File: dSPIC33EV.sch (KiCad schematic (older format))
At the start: 45 parts, among them J5 CONN_01X05, J6 test, J7 CONN_01X05, J8 CONN_COAXIAL, J9 DB9_Female_MountingHoles, SW1 SW_Push, U4 74LS04, U5 dsPIC33EV256GM002, U6 SN75451, U7 MAX232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

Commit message: 저항값설정
저항값 1차 설정
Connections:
- wire segments 158 -> 156
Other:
- note added: "RX Selection : R14 for optic interface, R12 RS232C interface. \nBetween them only one shoud be shorted"
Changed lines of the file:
@@
 Connection ~ 1900 9100
-Wire Wire Line
-	2650 9150 2650 9100
-Connection ~ 2650 9100
 Wire Wire Line
 	2400 9150 2400 9100
@@
 	2900 9500 2900 9450
 Connection ~ 1900 9500
-Wire Wire Line
-	2650 9450 2650 9500
-Connection ~ 2650 9500
 Wire Wire Line
 	2400 9450 2400 9500
@@
 Wire Wire Line
 	1750 7300 1900 7300
+Text Notes 8600 5550 0    60   ~ 0
+RX Selection : R14 for optic interface, R12 RS232C interface. \nBetween them only one shoud be shorted
 $EndSCHEMATC

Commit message: 전해콘덴서 foot print 변경
전해 콘덴서 변경
Bypass 콘데서 OPAMP에 추가 하여야 함
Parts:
- C28, C32, C34, C36, C39, C40, C41: footprint Capacitors_SMD:C_1812_HandSoldering -> USER:C_1812_HandSoldering_Polar
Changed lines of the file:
@@
 F 0 "C36" H 10775 6500 50  0000 L CNN
 F 1 "10uF" H 10775 6300 50  0000 L CNN
-F 2 "Capacitors_SMD:C_1812_HandSoldering" H 10750 6400 50  0001 C CNN
+F 2 "USER:C_1812_HandSoldering_Polar" H 10750 6400 50  0001 C CNN
 F 3 "" H 10750 6400 50  0001 C CNN
 	1    10750 6400
@@
 F 0 "C41" H 13125 7150 50  0000 L CNN
 F 1 "10uF" H 13125 6950 50  0000 L CNN
-F 2 "Capacitors_SMD:C_1812_HandSoldering" H 13100 7050 50  0001 C CNN
+F 2 "USER:C_1812_HandSoldering_Polar" H 13100 7050 50  0001 C CNN
 F 3 "" H 13100 7050 50  0001 C CNN
 	1    13100 7050
@@
 F 0 "C39" H 13075 6500 50  0000 L CNN
 F 1 "10uF" H 13075 6300 50  0000 L CNN
-F 2 "Capacitors_SMD:C_1812_HandSoldering" H 13050 6400 50  0001 C CNN
+F 2 "USER:C_1812_HandSoldering_Polar" H 13050 6400 50  0001 C CNN
 F 3 "" H 13050 6400 50  0001 C CNN
 	1    13050 6400
@@
 F 0 "C40" H 13125 6850 50  0000 L CNN
 F 1 "10uF" H 13125 6650 50  0000 L CNN
-F 2 "Capacitors_SMD:C_1812_HandSoldering" H 13100 6750 50  0001 C CNN
+F 2 "USER:C_1812_HandSoldering_Polar" H 13100 6750 50  0001 C CNN
 F 3 "" H 13100 6750 50  0001 C CNN
 	1    13100 6750
@@
 F 0 "C28" H 3525 3400 50  0000 L CNN
 F 1 "10uF" H 3525 3200 50  0000 L CNN
-F 2 "Capacitors_SMD:C_1812_HandSoldering" H 3500 3300 50  0001 C CNN
+F 2 "USER:C_1812_HandSoldering_Polar" H 3500 3300 50  0001 C CNN
 F 3 "" H 3500 3300 50  0001 C CNN
 	1    3500 3300
@@
 F 0 "C34" H 8875 4200 50  0000 L CNN
 F 1 "10uF" H 8875 4000 50  0000 L CNN
-F 2 "Capacitors_SMD:C_1812_HandSoldering" H 8850 4100 50  0001 C CNN
+F 2 "USER:C_1812_HandSoldering_Polar" H 8850 4100 50  0001 C CNN
 F 3 "" H 8850 4100 50  0001 C CNN
 	1    8850 4100
@@
 F 0 "C32" H 8575 2600 50  0000 L CNN
 F 1 "10uF" H 8575 2400 50  0000 L CNN
-F 2 "Capacitors_SMD:C_1812_HandSoldering" H 8550 2500 50  0001 C CNN
+F 2 "USER:C_1812_HandSoldering_Polar" H 8550 2500 50  0001 C CNN
 F 3 "" H 8550 2500 50  0001 C CNN
 	1    8550 2500

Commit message: switch 수정
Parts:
- removed R12, R14: 0, Resistors_SMD:R_0805_HandSoldering, symbol R
- added SW3: SW_DPDT_x2, USER:SW_E-Switch_EG2219_DPDT, symbol SW_DPDT_x2
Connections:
- wire segments 156 -> 162
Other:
- note removed: "RX Selection : R14 for optic interface, R12 RS232C interface. \nBetween them only one shoud be shorted"
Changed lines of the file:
@@
 Text Label 10750 7250 0    60   ~ 0
 TXD
-Text Label 10200 7650 0    60   ~ 0
+Text Label 9250 7550 0    60   ~ 0
 RXD
 Text Label 5750 3950 0    60   ~ 0
@@
 Text Label 11150 2900 0    60   ~ 0
 TXD
-Text Label 11200 4750 0    60   ~ 0
-RXD
 $Comp
 L GND #PWR068
@@
 	-1   0    0    -1
 $EndComp
-$Comp
-L R R12
-U 1 1 5B07D647
-P 10700 7650
-F 0 "R12" V 10780 7650 50  0000 C CNN
-F 1 "0" V 10700 7650 50  0000 C CNN
-F 2 "Resistors_SMD:R_0805_HandSoldering" V 10630 7650 50  0001 C CNN
-F 3 "" H 10700 7650 50  0001 C CNN
-	1    10700 7650
-	0    1    1    0
-$EndComp
-$Comp
-L R R14
-U 1 1 5B07EC31
-P 11600 4750
-F 0 "R14" V 11680 4750 50  0000 C CNN
-F 1 "0" V 11600 4750 50  0000 C CNN
-F 2 "Resistors_SMD:R_0805_HandSoldering" V 11530 4750 50  0001 C CNN
-F 3 "" H 11600 4750 50  0001 C CNN
-	1    11600 4750
-	0    1    1    0
-$EndComp
 NoConn ~ 12300 3100
 NoConn ~ 11500 3100
@@
 	11100 7250 10600 7250
 Wire Wire Line
-	10550 7650 10050 7650
+	9600 7550 9100 7550
 Wire Wire Line
 	12700 7250 14550 7250
@@
 Wire Wire Line
 	11500 2900 11000 2900
-Wire Wire Line
-	11000 4750 11450 4750
 Wire Wire Line
 	13050 2900 12800 2900
@@
 	11900 5150 11900 5200
 Wire Wire Line
-	10850 7650 11100 7650
-Wire Wire Line
-	11750 4750 12150 4750
+	10000 7650 11100 7650
+Wire Wire Line
+	10350 4750 12150 4750
 Wire Wire Line
 	9500 3750 9500 4300
@@
 Wire Wire Line
 	1750 7300 1900 7300
-Text Notes 8600 5550 0    60   ~ 0
-RX Selection : R14 for optic interface, R12 RS232C interface. \nBetween them only one shoud be shorted
+Wire Wire Line
+	10350 4750 10350 7950
+Wire Wire Line
+	10350 7450 10000 7450
+$Comp
+L SW_DPDT_x2 SW3
+U 1 1 5B1F38AC
+P 9800 7550
+F 0 "SW3" H 9800 7835 50  0000 C CNN
+F 1 "SW_DPDT_x2" H 9800 7744 50  0000 C CNN
+F 2 "USER:SW_E-Switch_EG2219_DPDT" H 9800 7550 50  0001 C CNN
+F 3 "" H 9800 7550 50  0001 C CNN
+	1    9800 7550
+	1    0    0    -1
+$EndComp
+$Comp
+L SW_DPDT_x2 SW3
+U 2 1 5B1F395D
+P 9750 8050
+F 0 "SW3" H 9750 8335 50  0000 C CNN
+F 1 "SW_DPDT_x2" H 9750 8244 50  0000 C CNN
+F 2 "USER:SW_E-Switch_EG2219_DPDT" H 9750 8050 50  0001 C CNN
+F 3 "" H 9750 8050 50  0001 C CNN
+	2    9750 8050
+	1    0    0    -1
+$EndComp
+Wire Wire Line
+	9550 8050 9450 8050
+Wire Wire Line
+	9450 8050 9450 7550
+Connection ~ 9450 7550
+Wire Wire Line
+	10350 7950 9950 7950
+Connection ~ 10350 7450
+Wire Wire Line
+	9950 8150 10500 8150
+Wire Wire Line
+	10500 8150 10500 7650
+Connection ~ 10500 7650
 $EndSCHEMATC

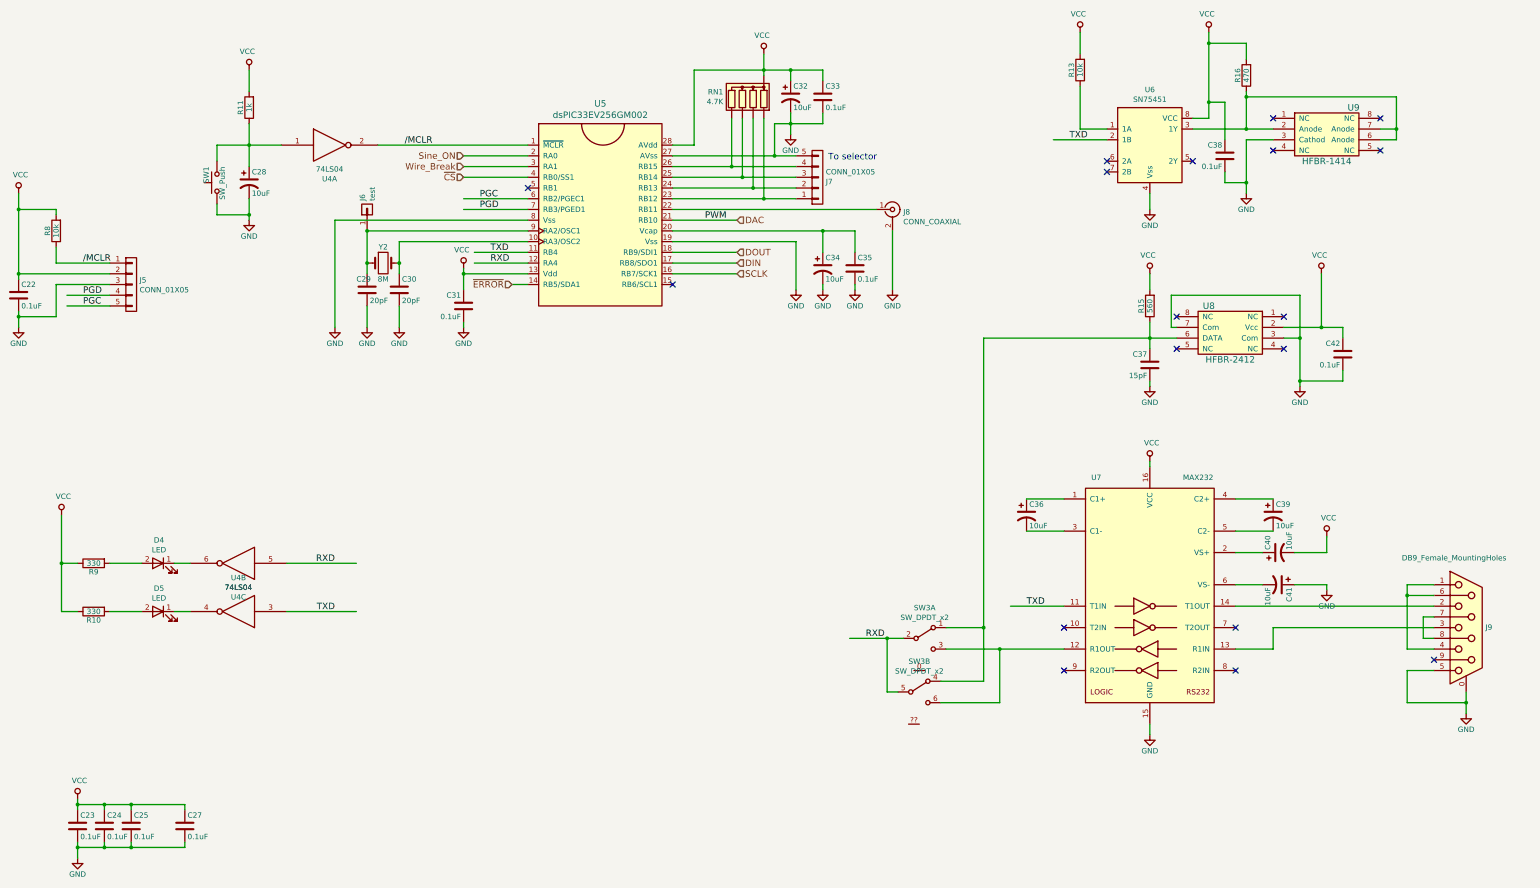
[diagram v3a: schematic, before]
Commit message: Selector Numbering
Selector numbering
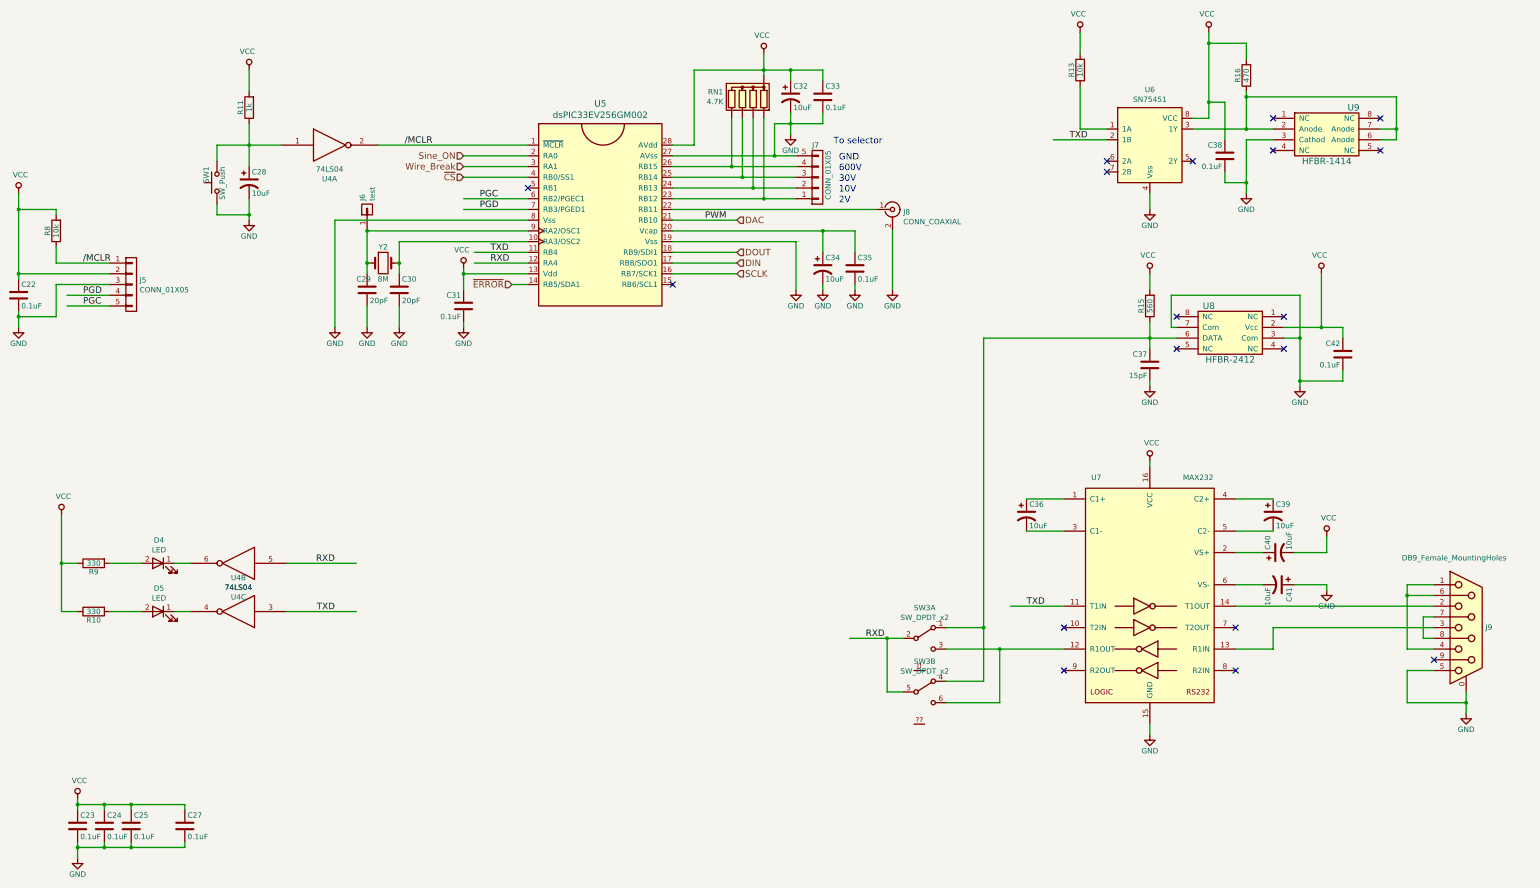
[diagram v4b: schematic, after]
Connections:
- wire segments 162 -> 205
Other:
- note added: "10V"
- note added: "2V"
- note added: "30V"
- note added: "600V"
- note added: "GND"
- moved on the sheet: SW3B
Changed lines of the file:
@@
 U 1 1 5B04EF67
 P 8800 3250
-F 0 "J7" H 8878 3291 50  0000 L CNN
-F 1 "CONN_01X05" H 8878 3200 50  0000 L CNN
+F 0 "J7" H 8750 2950 50  0000 L CNN
+F 1 "CONN_01X05" V 8900 3000 50  0000 L CNN
 F 2 "USER:M53259-5" H 8800 3250 50  0001 C CNN
 F 3 "" H 8800 3250 50  0001 C CNN
@@
 	1    0    0    1
 $EndComp
-Text Notes 8900 3100 0    60   ~ 0
+Text Notes 8950 2950 0    60   ~ 0
 To selector
 $Comp
@@
 	7450 4050 8050 4050
 Wire Wire Line
-	14850 8050 14850 8250
+	14850 8050 14850 8150
+Wire Wire Line
+	14850 8150 14850 8250
 Wire Wire Line
 	13050 7450 14550 7450
@@
 Connection ~ 14850 8150
 Wire Wire Line
-	14300 7050 14300 7650
+	14300 7050 14300 7150
+Wire Wire Line
+	14300 7150 14300 7650
 Wire Wire Line
 	14550 7350 14450 7350
@@
 	11100 7250 10600 7250
 Wire Wire Line
-	9600 7550 9100 7550
+	9600 7550 9450 7550
+Wire Wire Line
+	9450 7550 9100 7550
 Wire Wire Line
 	12700 7250 14550 7250
@@
 	11900 5900 11900 5950
 Wire Wire Line
-	1900 9450 1900 9600
-Wire Wire Line
-	1900 9050 1900 9150
-Wire Wire Line
-	1900 9100 2900 9100
+	1900 9450 1900 9500
+Wire Wire Line
+	1900 9500 1900 9600
+Wire Wire Line
+	1900 9050 1900 9100
+Wire Wire Line
+	1900 9100 1900 9150
+Wire Wire Line
+	1900 9100 2150 9100
+Wire Wire Line
+	2150 9100 2400 9100
+Wire Wire Line
+	2400 9100 2900 9100
 Wire Wire Line
 	2900 9100 2900 9150
@@
 Connection ~ 2150 9100
 Wire Wire Line
-	1900 9500 2900 9500
+	1900 9500 2150 9500
+Wire Wire Line
+	2150 9500 2400 9500
+Wire Wire Line
+	2400 9500 2900 9500
 Wire Wire Line
 	2900 9500 2900 9450
@@
 Connection ~ 2150 9500
 Wire Wire Line
-	1350 4500 1350 4650
+	1350 4500 1350 4550
+Wire Wire Line
+	1350 4550 1350 4650
 Wire Wire Line
 	1800 4350 2200 4350
@@
 Connection ~ 1350 4150
 Wire Wire Line
-	1350 3400 1350 4200
+	1350 3400 1350 3550
+Wire Wire Line
+	1350 3550 1350 4150
+Wire Wire Line
+	1350 4150 1350 4200
 Wire Wire Line
 	1700 4550 1350 4550
@@
 	5500 4150 6100 4150
 Wire Wire Line
-	5500 4100 5500 4300
+	5500 4100 5500 4150
+Wire Wire Line
+	5500 4150 5500 4300
 Connection ~ 5500 4150
 Wire Wire Line
-	4900 3850 4900 4150
+	4900 3850 4900 4050
+Wire Wire Line
+	4900 4050 4900 4150
 Wire Wire Line
 	4600 3750 6100 3750
 Wire Wire Line
-	4600 3750 4600 4150
+	4600 3750 4600 4050
+Wire Wire Line
+	4600 4050 4600 4150
 Wire Wire Line
 	6100 3650 4300 3650
@@
 	4700 2950 6100 2950
 Wire Wire Line
-	12800 2450 12800 2800
-Wire Wire Line
-	12300 2800 13050 2800
+	12800 2450 12800 2500
+Wire Wire Line
+	12800 2500 12800 2800
+Wire Wire Line
+	12300 2800 12800 2800
+Wire Wire Line
+	12800 2800 13050 2800
 Wire Wire Line
 	14050 2800 14200 2800
 Wire Wire Line
-	14200 2500 14200 2900
+	14200 2500 14200 2800
+Wire Wire Line
+	14200 2800 14200 2900
 Wire Wire Line
 	14200 2900 14050 2900
@@
 Connection ~ 12800 2800
 Wire Wire Line
-	12450 1900 12450 2700
+	12450 1900 12450 2000
+Wire Wire Line
+	12450 2000 12450 2550
+Wire Wire Line
+	12450 2550 12450 2700
 Wire Wire Line
 	12450 2700 12300 2700
@@
 	13050 2900 12800 2900
 Wire Wire Line
-	12800 2900 12800 3400
+	12800 2900 12800 3300
+Wire Wire Line
+	12800 3300 12800 3400
 Wire Wire Line
 	12600 3200 12600 3300
@@
 	11900 4300 11900 4150
 Wire Wire Line
-	11900 4600 11900 4850
+	11900 4600 11900 4750
+Wire Wire Line
+	11900 4750 11900 4850
 Connection ~ 11900 4750
 Wire Wire Line
@@
 	12100 4350 13300 4350
 Wire Wire Line
-	13300 4350 13300 5200
+	13300 4350 13300 4750
+Wire Wire Line
+	13300 4750 13300 5150
+Wire Wire Line
+	13300 5150 13300 5200
 Wire Wire Line
 	13150 4750 13300 4750
@@
 	13500 4150 13500 4650
 Wire Wire Line
-	13150 4650 13700 4650
+	13150 4650 13500 4650
+Wire Wire Line
+	13500 4650 13700 4650
 Wire Wire Line
 	13700 5050 13700 5150
@@
 Connection ~ 13300 5150
 Wire Wire Line
-	1750 6400 1750 7300
+	1750 6400 1750 6850
+Wire Wire Line
+	1750 6850 1750 7300
 Wire Wire Line
 	2950 7300 2800 7300
@@
 	3500 2250 3500 2450
 Wire Wire Line
-	3500 2750 3500 3150
-Wire Wire Line
-	3200 2950 3800 2950
+	3500 2750 3500 2950
+Wire Wire Line
+	3500 2950 3500 3150
+Wire Wire Line
+	3200 2950 3500 2950
+Wire Wire Line
+	3500 2950 3800 2950
 Connection ~ 3500 2950
 Wire Wire Line
-	3500 3450 3500 3650
+	3500 3450 3500 3600
+Wire Wire Line
+	3500 3600 3500 3650
 Wire Wire Line
 	3200 3100 3200 2950
@@
 	8850 4250 8850 4300
 Wire Wire Line
-	7450 3750 9150 3750
+	7450 3750 8850 3750
+Wire Wire Line
+	8850 3750 9150 3750
 Wire Wire Line
 	8850 3950 8850 3750
@@
 	9150 3750 9150 3950
 Wire Wire Line
-	8300 2100 8300 2300
+	8300 2100 8300 2250
+Wire Wire Line
+	8300 2250 8300 2300
 Wire Wire Line
 	8000 2700 8000 3150
 Wire Wire Line
-	7450 3150 8600 3150
+	7450 3150 8000 3150
+Wire Wire Line
+	8000 3150 8600 3150
 Wire Wire Line
 	8100 2700 8100 3250
@@
 Connection ~ 8300 3450
 Wire Wire Line
-	7450 3250 8600 3250
-Wire Wire Line
-	7450 3350 8600 3350
-Wire Wire Line
-	7450 3450 8600 3450
+	7450 3250 8100 3250
+Wire Wire Line
+	8100 3250 8600 3250
+Wire Wire Line
+	7450 3350 8200 3350
+Wire Wire Line
+	8200 3350 8600 3350
+Wire Wire Line
+	7450 3450 8300 3450
+Wire Wire Line
+	8300 3450 8600 3450
 Wire Wire Line
 	8850 2750 8850 2650
 Wire Wire Line
-	8550 2650 8550 2850
-Wire Wire Line
-	7650 2250 8850 2250
+	8550 2650 8550 2750
+Wire Wire Line
+	8550 2750 8550 2850
+Wire Wire Line
+	7650 2250 8300 2250
+Wire Wire Line
+	8300 2250 8550 2250
+Wire Wire Line
+	8550 2250 8850 2250
 Wire Wire Line
 	11900 3400 11900 3550
@@
 	7450 2950 7650 2950
 Wire Wire Line
-	7450 3050 8600 3050
+	7450 3050 8400 3050
+Wire Wire Line
+	8400 3050 8600 3050
 Wire Wire Line
 	8400 3050 8400 2750
@@
 Connection ~ 8550 2750
 Wire Wire Line
-	8400 2750 8850 2750
+	8400 2750 8550 2750
+Wire Wire Line
+	8550 2750 8850 2750
 Wire Wire Line
 	11900 5150 11900 5200
 Wire Wire Line
-	10000 7650 11100 7650
-Wire Wire Line
-	10350 4750 12150 4750
+	10000 7650 10500 7650
+Wire Wire Line
+	10500 7650 11100 7650
+Wire Wire Line
+	10350 4750 11900 4750
+Wire Wire Line
+	11900 4750 12150 4750
 Wire Wire Line
 	9500 3750 9500 4300
@@
 	1750 7300 1900 7300
 Wire Wire Line
-	10350 4750 10350 7950
+	10350 4750 10350 7450
+Wire Wire Line
+	10350 7450 10350 7950
 Wire Wire Line
 	10350 7450 10000 7450
@@
 L SW_DPDT_x2 SW3
 U 2 1 5B1F395D
-P 9750 8050
-F 0 "SW3" H 9750 8335 50  0000 C CNN
-F 1 "SW_DPDT_x2" H 9750 8244 50  0000 C CNN
-F 2 "USER:SW_E-Switch_EG2219_DPDT" H 9750 8050 50  0001 C CNN
-F 3 "" H 9750 8050 50  0001 C CNN
-	2    9750 8050
+P 9800 8050
+F 0 "SW3" H 9800 8335 50  0000 C CNN
+F 1 "SW_DPDT_x2" H 9800 8244 50  0000 C CNN
+F 2 "USER:SW_E-Switch_EG2219_DPDT" H 9800 8050 50  0001 C CNN
+F 3 "" H 9800 8050 50  0001 C CNN
+	2    9800 8050
 	1    0    0    -1
 $EndComp
 Wire Wire Line
-	9550 8050 9450 8050
+	9600 8050 9450 8050
 Wire Wire Line
 	9450 8050 9450 7550
 Connection ~ 9450 7550
 Wire Wire Line
-	10350 7950 9950 7950
+	10350 7950 10000 7950
 Connection ~ 10350 7450
 Wire Wire Line
-	9950 8150 10500 8150
+	10000 8150 10500 8150
 Wire Wire Line
 	10500 8150 10500 7650
 Connection ~ 10500 7650
+Text Notes 9000 3200 0    60   ~ 0
+600V
+Text Notes 9000 3300 0    60   ~ 0
+30V
+Text Notes 9000 3400 0    60   ~ 0
+10V
+Text Notes 9000 3500 0    60   ~ 0
+2V
+Text Notes 9000 3100 0    60   ~ 0
+GND
 $EndSCHEMATC

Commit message: 0805_넓히기
기타 수정
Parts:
- U4: footprint Housings_SOIC:SOIC-14_3.9x8.7mm_Pitch1.27mm -> Housings_DIP:DIP-14_W7.62mm_Socket
- U6: value SN75451 -> SN75452
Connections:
- wire segments 205 -> 165
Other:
- moved on the sheet: C22, C23, C24, C25, C27, C28, C29, C30, C31, C32, C33, C34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

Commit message: 2차PCB
U22 포함
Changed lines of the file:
@@
 	0    -1   1    0
 $EndComp
-Text Label 4300 7550 2    60   ~ 0
+Text Label 5250 8550 2    60   ~ 0
 TXD
-Text Label 4300 7100 2    60   ~ 0
+Text Label 5250 8100 2    60   ~ 0
 RXD
 $Comp

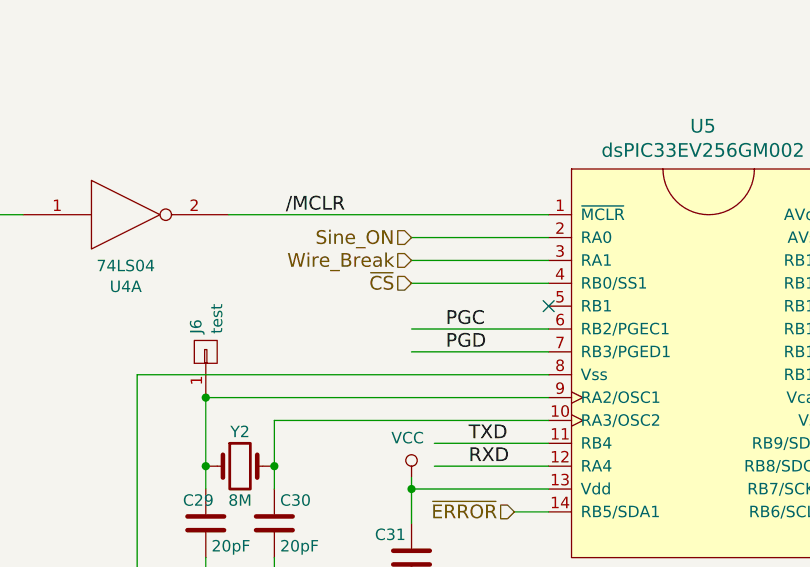
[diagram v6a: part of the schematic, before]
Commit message: 4차 PCB
U23 Wire Breakage Relay 추가
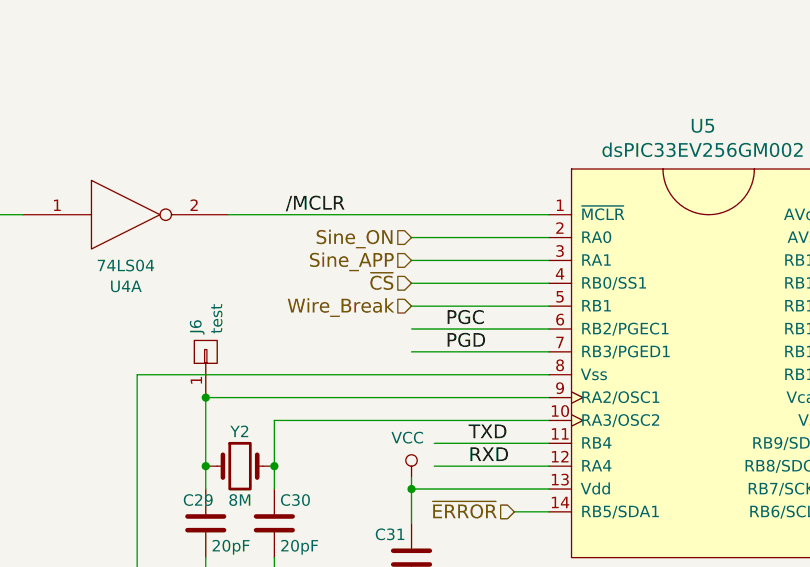
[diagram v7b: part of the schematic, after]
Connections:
- net labels added: Sine_APP
- wire segments 165 -> 166
- no-connect marks 18 -> 17
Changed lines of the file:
@@
 Sine_ON
 Text HLabel 5200 3000 0    60   Input ~ 0
-Wire_Break
+Sine_APP
 $Comp
 L CONN_01X05 J7
@@
 NoConn ~ 13150 4850
 NoConn ~ 13150 4550
-NoConn ~ 5800 3200
 NoConn ~ 7150 4100
 $Comp
@@
 	9700 8350 9350 8350
 Connection ~ 9350 8350
+Text HLabel 5200 3200 0    60   Input ~ 0
+Wire_Break
+Wire Wire Line
+	5800 3200 5200 3200
 $EndSCHEMATC
